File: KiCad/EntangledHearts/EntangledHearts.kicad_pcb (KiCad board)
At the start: 2 copper layers, 63 parts, among them J1 Conn_01x05_Pin, J2 MPU, J3 USB4135-GF-A, J4 OLED Display, J5 Conn_01x05_Pin, J6 Conn_01x05_Pin, Q1 SFH_3711, Q3 2N7002, Q4 2N7002, U1 ESP32-S3-WROOM-1, U2 MCP73831-2-OT, U3 TC1185-xCT

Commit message: ADD: first pcbs added
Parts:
- removed S_BOOT1, S_TXD2: TXD, TestPoint:TestPoint_Pad_1.0x1.0mm
- removed S_BOOT2: Boot, TestPoint:TestPoint_Pad_1.0x1.0mm
- removed S_EN1, S_RXD2: RXD, TestPoint:TestPoint_Pad_1.0x1.0mm
- removed S_EN2: Enabled, TestPoint:TestPoint_Pad_1.0x1.0mm
- removed S_RXD1: DTR, TestPoint:TestPoint_Pad_1.0x1.0mm
- removed S_TXD1: RTS, TestPoint:TestPoint_Pad_1.0x1.0mm
- removed TPS_GND1, TPS_GND2: GND, TestPoint:TestPoint_Pad_1.0x1.0mm
- +Bat1: renamed from TP16; footprint TestPoint:TestPoint_Pad_1.0x1.0mm -> TestPoint:TestPoint_Pad_2.5x2.5mm
- -Bat1: renamed from TP4; footprint TestPoint:TestPoint_Pad_1.0x1.0mm -> TestPoint:TestPoint_Pad_2.5x2.5mm
- Seriell_Flash1: renamed from J6; value Conn_01x05_Pin -> Flash
- Seriell_Input1: renamed from J1; value Conn_01x05_Pin -> Input
- Seriell_Output1: renamed from J5; value Conn_01x05_Pin -> Output
- moved S2 121.1 mm to (226.1, 103.9)
- moved C12 109.7 mm to (239.7, 121.5)
- moved C15 109.2 mm to (242.2, 116.4)
- moved U3 101.8 mm to (216.0, 114.8)
- moved C14 101.6 mm to (234.9, 111.3)
- moved C13 101.3 mm to (230.8, 117.7)
- moved R7 94.9 mm to (232.1, 130.4)
- moved U2 87.8 mm to (201.0, 112.7), turned to 90 degrees
- moved J3 84.3 mm to (187.3, 115.2), turned to -90 degrees
- moved Seriell_Output1 84.0 mm to (213.0, 44.5)
- moved R9 83.9 mm to (201.9, 40.6)
- moved R10 79.5 mm to (191.8, 40.6)
- moved -Bat1 79.2 mm to (208.3, 124.0)
- moved C11 77.6 mm to (205.7, 117.7), turned to -90 degrees
- moved +Bat1 73.4 mm to (208.3, 106.3)
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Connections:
- C8 pad 2: Net-(U1-GPIO0/BOOT) -> Net-(Seriell_Flash1-Pin_1)
- C9 pad 2: Net-(U1-EN) -> Net-(Seriell_Flash1-Pin_4)
- R5 pad 1: Net-(U1-GPIO0/BOOT) -> Net-(Seriell_Flash1-Pin_1)
- R6 pad 1: Net-(U1-EN) -> Net-(Seriell_Flash1-Pin_4)
- Seriell_Flash1 pad 1: unconnected-(J6-Pin_1-Pad1) -> Net-(Seriell_Flash1-Pin_1)
- Seriell_Flash1 pad 2: unconnected-(J6-Pin_2-Pad2) -> Net-(Seriell_Flash1-Pin_2)
- Seriell_Flash1 pad 3: unconnected-(J6-Pin_3-Pad3) -> Net-(Seriell_Flash1-Pin_3)
- Seriell_Flash1 pad 4: unconnected-(J6-Pin_4-Pad4) -> Net-(Seriell_Flash1-Pin_4)
- Seriell_Flash1 pad 5: unconnected-(J6-Pin_5-Pad5) -> GND
- Seriell_Input1 pad 1: unconnected-(J1-Pin_1-Pad1) -> Net-(Q4-S)
- Seriell_Input1 pad 2: unconnected-(J1-Pin_2-Pad2) -> Net-(Q3-S)
- Seriell_Input1 pad 3: unconnected-(J1-Pin_3-Pad3) -> Net-(Seriell_Input1-Pin_3)
- Seriell_Input1 pad 4: unconnected-(J1-Pin_4-Pad4) -> Net-(Seriell_Input1-Pin_4)
- Seriell_Input1 pad 5: unconnected-(J1-Pin_5-Pad5) -> Net-(Seriell_Input1-Pin_5)
- Seriell_Output1 pad 1: unconnected-(J5-Pin_1-Pad1) -> Net-(Q3-D)
- Seriell_Output1 pad 2: unconnected-(J5-Pin_2-Pad2) -> Net-(Seriell_Input1-Pin_3)
- Seriell_Output1 pad 3: unconnected-(J5-Pin_3-Pad3) -> Net-(Seriell_Input1-Pin_4)
- Seriell_Output1 pad 4: unconnected-(J5-Pin_4-Pad4) -> Net-(Q4-D)
- Seriell_Output1 pad 5: unconnected-(J5-Pin_5-Pad5) -> Net-(Seriell_Input1-Pin_5)
- U1 pad 27: Net-(U1-GPIO0/BOOT) -> Net-(Seriell_Flash1-Pin_1)
- U1 pad 3: Net-(U1-EN) -> Net-(Seriell_Flash1-Pin_4)
- U1 pad 36: Net-(U1-U0RXD/GPIO44/CLK_OUT2) -> Net-(Seriell_Flash1-Pin_2)
- U1 pad 37: Net-(U1-U0TXD/GPIO43/CLK_OUT1) -> Net-(Seriell_Flash1-Pin_3)
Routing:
- net GND: track 0.00 -> 55.2 mm
- net Net-(Seriell_Input1-Pin_3): track 0.00 -> 36.6 mm, vias 0 -> 2
- net Net-(Seriell_Input1-Pin_5): track 0.00 -> 32.2 mm
- net Net-(Seriell_Input1-Pin_4): track 0.00 -> 30.0 mm, vias 0 -> 2
- net Net-(Q4-S): track 0.00 -> 29.8 mm, vias 0 -> 3
- net Net-(Q3-S): track 0.00 -> 26.3 mm
- net Net-(U2-V_{DD}): track 0.00 -> 25.8 mm
- net Net-(Q4-D): track 0.00 -> 23.9 mm
- net Net-(Q3-D): track 0.00 -> 15.5 mm
- net Net-(U2-V_{BAT}): track 0.00 -> 15.1 mm
- net Net-(Q4-G): track 0.00 -> 4.67 mm
- net Net-(Q3-G): track 0.00 -> 4.67 mm
- net Net-(D7-A): track 0.00 -> 3.04 mm
- net Net-(D7-K): track 0.00 -> 2.24 mm

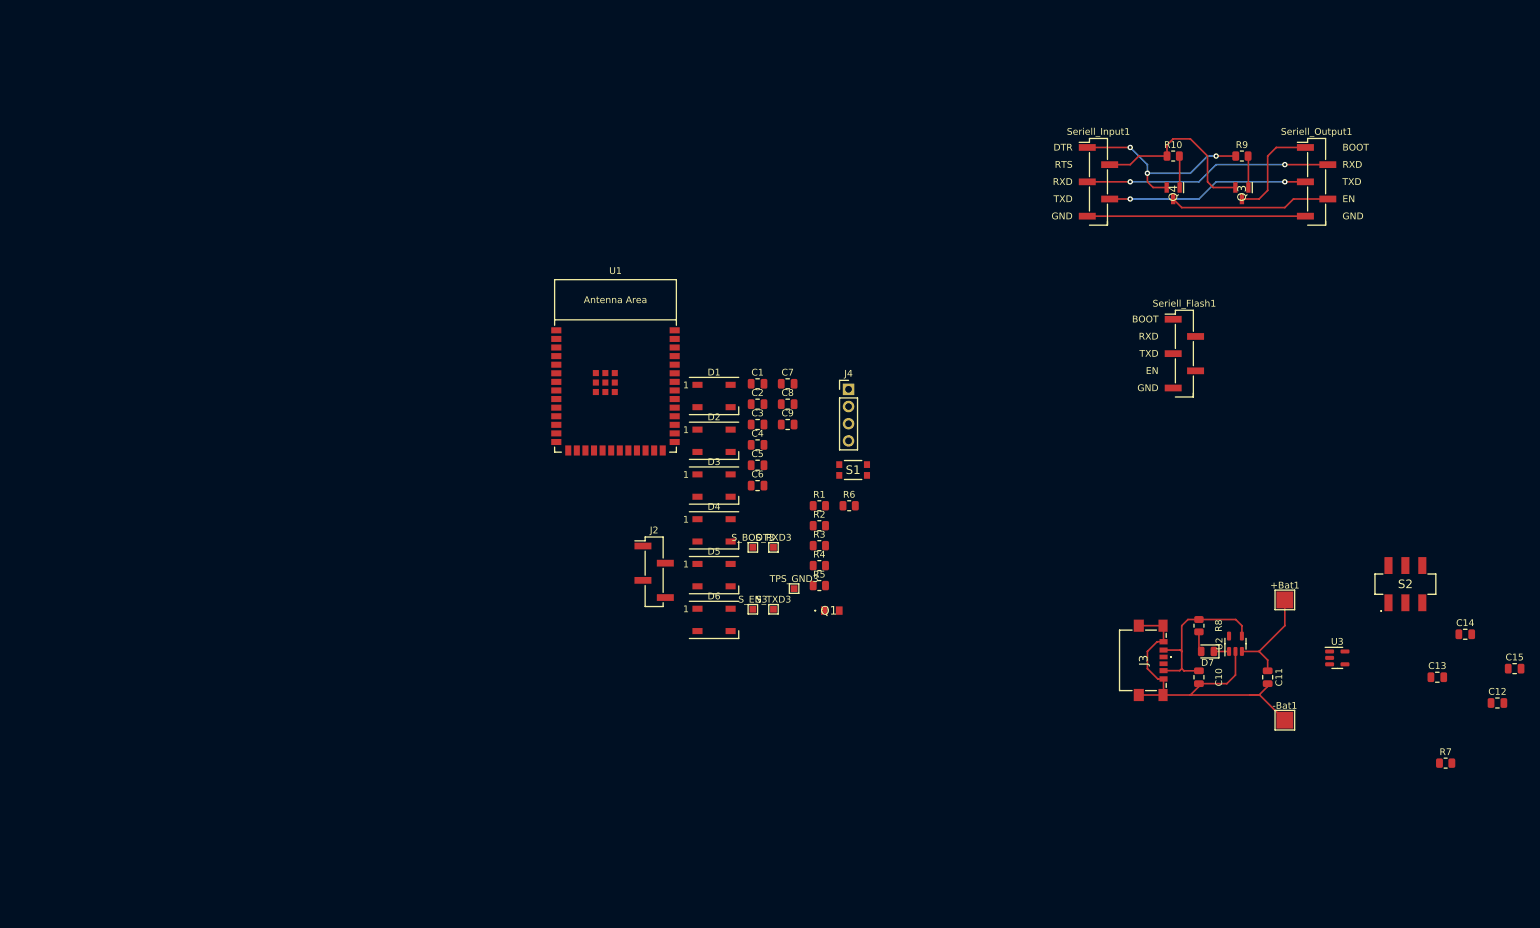
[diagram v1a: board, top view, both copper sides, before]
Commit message: CHG cleanup of Schematics done
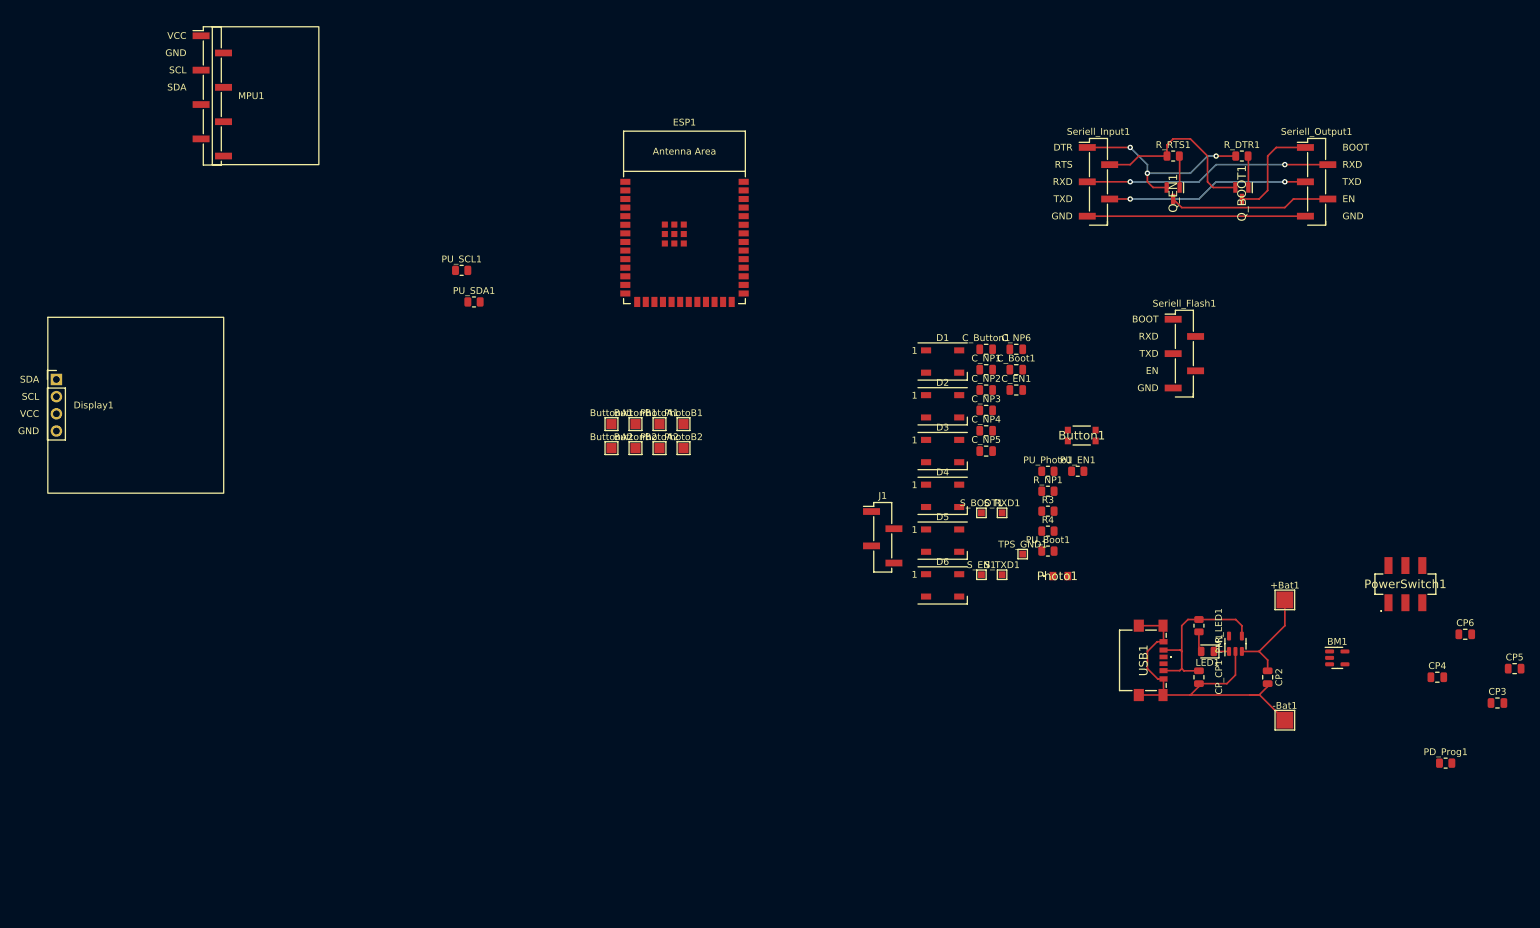
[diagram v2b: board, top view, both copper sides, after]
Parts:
- added ButtonA1: ButtonA1, TestPoint:TestPoint_Pad_1.5x1.5mm, F.Cu at (108.7, 80.3)
- added ButtonA2: ButtonA2, TestPoint:TestPoint_Pad_1.5x1.5mm, F.Cu at (108.7, 83.8)
- added ButtonB1: ButtonB1, TestPoint:TestPoint_Pad_1.5x1.5mm, F.Cu at (112.3, 80.3)
- added ButtonB2: ButtonB2, TestPoint:TestPoint_Pad_1.5x1.5mm, F.Cu at (112.3, 83.8)
- added MPU1: Conn_01x08_Pin, Connector_PinHeader_2.54mm:PinHeader_1x08_P2.54mm_Vertical_SMD_Pin1Left, F.Cu at (49.7, 31.8)
- added PU_SCL1: 10kΩ, Resistor_SMD:R_0805_2012Metric, F.Cu at (86.6, 57.5)
- added PU_SDA1: 10kΩ, Resistor_SMD:R_0805_2012Metric, F.Cu at (88.4, 62.2)
- added PhotoA1: PhotoA1, TestPoint:TestPoint_Pad_1.5x1.5mm, F.Cu at (115.8, 80.3)
- added PhotoA2: PhotoA2, TestPoint:TestPoint_Pad_1.5x1.5mm, F.Cu at (115.8, 83.8)
- added PhotoB1: PhotoB1, TestPoint:TestPoint_Pad_1.5x1.5mm, F.Cu at (119.4, 80.3)
- added PhotoB2: PhotoB2, TestPoint:TestPoint_Pad_1.5x1.5mm, F.Cu at (119.4, 83.8)
- D1: value WS2812B -> NP1
- D2: value WS2812B -> NP2
- D3: value WS2812B -> NP3
- D4: value WS2812B -> NP4
- D5: value WS2812B -> NP5
- D6: value WS2812B -> NP6
- moved Display1 117.1 mm to (26.7, 73.7)
- moved Button1 34.2 mm to (178.2, 82.0)
- moved C_Button1 34.2 mm to (164.1, 69.2)
- moved C_NP1 34.2 mm to (164.1, 72.2)
- moved C_NP2 34.2 mm to (164.1, 75.2)
- moved C_NP3 34.2 mm to (164.1, 78.2)
- moved C_NP4 34.2 mm to (164.1, 81.2)
- moved C_NP5 34.2 mm to (164.1, 84.3)
- moved J1 34.2 mm to (148.8, 97.0)
- moved S_BOOT1 34.2 mm to (163.4, 93.4)
- moved S_EN1 34.2 mm to (163.4, 102.5)
- moved TPS_GND1 34.2 mm to (169.5, 99.5)
- moved D1 34.2 mm to (157.7, 71.0)
- moved D2 34.2 mm to (157.7, 77.6)
- moved D3 34.2 mm to (157.7, 84.3)
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- renumbered U3 to BM1, S1 to Button1, C11 to CP2, C12 to CP3, C13 to CP4, C15 to CP5, C14 to CP6, C10 to CP_CP1, C8 to C_Boot1, C1 to C_Button1, C9 to C_EN1, C2 to C_NP1, C3 to C_NP2, C4 to C_NP3, C5 to C_NP4, C6 to C_NP5, C7 to C_NP6, J4 to Display1, U1 to ESP1, J2 to J1, D7 to LED1, R7 to PD_Prog1, U2 to PM1, R5 to PU_Boot1, R6 to PU_EN1, R1 to PU_Photo1, Q1 to Photo1, S2 to PowerSwitch1, Q3 to Q_BOOT1, Q4 to Q_EN1, R9 to R_DTR1, R8 to R_LED1, R2 to R_NP1, R10 to R_RTS1, S_BOOT3 to S_BOOT1, S_EN3 to S_EN1, S_RXD3 to S_RXD1, S_TXD3 to S_TXD1, TPS_GND3 to TPS_GND1, J3 to USB1
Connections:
- net Net-(Seriell_Flash1-Pin_1) renamed Boot
- net Net-(Seriell_Flash1-Pin_4) renamed EN
- net Net-(U1-GPIO21) renamed NeoPixel
- Button1 pad 3: GND -> Net-(Button1-Pad3)
- Button1 pad 4: Net-(U1-GPIO1/TOUCH1/ADC1_CH0) -> Net-(Button1-Pad4)
- C_Button1 pad 1: Net-(U1-GPIO1/TOUCH1/ADC1_CH0) -> Button
- Display1 pad 1: GND -> SDA
- Display1 pad 2: +4V -> SCL
- Display1 pad 3: Net-(J2-Pin_2) -> +4V
- Display1 pad 4: Net-(J2-Pin_1) -> GND
- ESP1 pad 19: Net-(J2-Pin_1) -> SCL
- ESP1 pad 20: Net-(J2-Pin_2) -> SDA
- ESP1 pad 36: Net-(Seriell_Flash1-Pin_2) -> TXD
- ESP1 pad 37: Net-(Seriell_Flash1-Pin_3) -> RXD
- ESP1 pad 38: Net-(Q1-C) -> Photo
- ESP1 pad 39: Net-(U1-GPIO1/TOUCH1/ADC1_CH0) -> Button
- J1 pad 1: Net-(J2-Pin_1) -> SCL
- J1 pad 2: Net-(J2-Pin_2) -> SDA
- PU_Photo1 pad 1: Net-(Q1-C) -> Photo
- PU_Photo1 pad 2: +3.3V -> unconnected-(PU_Photo1-Pad2)
- Photo1 pad 1: GND -> Net-(Photo1-E)
- Photo1 pad 2: Net-(Q1-C) -> Net-(Photo1-C)
- R3 pad 1: Net-(J2-Pin_1) -> SCL
- R4 pad 1: Net-(J2-Pin_2) -> SDA
- Seriell_Flash1 pad 2: Net-(Seriell_Flash1-Pin_2) -> RXD
- Seriell_Flash1 pad 3: Net-(Seriell_Flash1-Pin_3) -> TXD

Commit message: ADD: further progress
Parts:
- removed J1: MPU, Connector_PinHeader_2.54mm:PinHeader_1x04_P2.54mm_Vertical_SMD_Pin1Left
- removed R3, R4: 10kΩ, Resistor_SMD:R_0805_2012Metric
- removed S_BOOT1: Boot, TestPoint:TestPoint_Pad_1.0x1.0mm
- removed S_EN1: Enabled, TestPoint:TestPoint_Pad_1.0x1.0mm
- removed S_RXD1: RXD (twist), TestPoint:TestPoint_Pad_1.0x1.0mm
- removed S_TXD1: TXD (twist), TestPoint:TestPoint_Pad_1.0x1.0mm
- removed TPS_GND1: GND, TestPoint:TestPoint_Pad_1.0x1.0mm
- added GND1: GND1, TestPoint:TestPoint_Pad_1.5x1.5mm, B.Cu at (96.5, 20.3)
- added GND2: GND2, TestPoint:TestPoint_Pad_1.5x1.5mm, B.Cu at (207.0, 80.4)
- added NeoPixel1: NeoPixel1, TestPoint:TestPoint_Pad_1.5x1.5mm, B.Cu at (88.9, 20.3)
- added NeoPixel2: NeoPixel2, TestPoint:TestPoint_Pad_1.5x1.5mm, B.Cu at (222.2, 80.4)
- added SCL1: SCL1, TestPoint:TestPoint_Pad_1.5x1.5mm, B.Cu at (85.1, 20.3)
- added SCL2: SCL2, TestPoint:TestPoint_Pad_1.5x1.5mm, B.Cu at (214.6, 80.4)
- added SDA1: SDA1, TestPoint:TestPoint_Pad_1.5x1.5mm, B.Cu at (81.3, 20.3)
- added SDA2: SDA2, TestPoint:TestPoint_Pad_1.5x1.5mm, B.Cu at (218.4, 80.4)
- added VCC1: VCC1, TestPoint:TestPoint_Pad_1.5x1.5mm, B.Cu at (92.7, 20.3)
- added VCC2: VCC2, TestPoint:TestPoint_Pad_1.5x1.5mm, B.Cu at (210.8, 80.4)
- +Bat1, -Bat1, ButtonA1, ButtonA2, ButtonB1, ButtonB2, CP_CP1, C_Button1, C_NP1, C_NP2, C_NP3, C_NP4, C_NP5, C_NP6, PU_Photo1, PhotoA1, PhotoA2, PhotoB1, PhotoB2, R_NP1: moved to B.Cu
- moved Display1 191.8 mm to (218.4, 75.3), turned to -90 degrees
- moved CP3 190.1 mm to (54.7, 78.1)
- moved CP6 189.9 mm to (48.0, 78.1)
- moved CP5 186.0 mm to (59.7, 80.6)
- moved PowerSwitch1 182.3 mm to (44.3, 90.8), turned to 90 degrees
- moved PD_Prog1 175.3 mm to (61.0, 92.0), turned to -90 degrees
- moved CP4 172.6 mm to (61.0, 87.0), turned to 90 degrees
- moved -Bat1 169.7 mm to (40.7, 97.1), turned to 180 degrees
- moved BM1 161.1 mm to (57.3, 87.0)
- moved CP_CP1 151.2 mm to (45.8, 97.1), turned to 180 degrees
- moved +Bat1 150.1 mm to (58.5, 97.1), turned to 180 degrees
- moved LED1 146.6 mm to (52.1, 90.8), turned to 90 degrees
- moved PM1 145.1 mm to (57.3, 92.4), turned to 0 degrees
- moved R_LED1 144.5 mm to (53.4, 84.4), turned to 180 degrees
- moved CP2 143.9 mm to (63.5, 95.8), turned to 90 degrees
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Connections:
- Button1 pad 2: unconnected-(Button1-Pad2) -> Net-(Button1-Pad2)
- Button1 pad 3: Net-(Button1-Pad3) -> unconnected-(Button1-Pad3)
- ButtonB2 pad 1: Net-(Button1-Pad3) -> Net-(Button1-Pad2)
- C_NP1 pad 1: +4V -> VCC_Top
- C_NP1 pad 2: GND -> GND_Top
- C_NP2 pad 1: +4V -> VCC_Top
- C_NP2 pad 2: GND -> GND_Top
- C_NP3 pad 1: +4V -> VCC_Top
- C_NP3 pad 2: GND -> GND_Top
- C_NP4 pad 1: +4V -> VCC_Top
- C_NP4 pad 2: GND -> GND_Top
- C_NP5 pad 1: +4V -> VCC_Top
- C_NP5 pad 2: GND -> GND_Top
- C_NP6 pad 1: +4V -> VCC_Top
- C_NP6 pad 2: GND -> GND_Top
- D1 pad 1: +4V -> VCC_Top
- D1 pad 3: GND -> GND_Top
- D2 pad 1: +4V -> VCC_Top
- D2 pad 3: GND -> GND_Top
- D3 pad 1: +4V -> VCC_Top
- D3 pad 3: GND -> GND_Top
- D4 pad 1: +4V -> VCC_Top
- D4 pad 3: GND -> GND_Top
- D5 pad 1: +4V -> VCC_Top
- D5 pad 3: GND -> GND_Top
- D6 pad 1: +4V -> VCC_Top
- D6 pad 3: GND -> GND_Top
- Display1 pad 1: SDA -> SDA_Top
- Display1 pad 2: SCL -> SCL_Top
- Display1 pad 3: +4V -> VCC_Top
- Display1 pad 4: GND -> GND_Top
- ESP1 pad 19: SCL -> SDA_Bottom
- ESP1 pad 20: SDA -> SCL_Bottom
- ESP1 pad 23: NeoPixel -> NeoPixelBottom
- MPU1 pad 3: SCL -> SCL_Bottom
- MPU1 pad 4: SDA -> SDA_Bottom
- PU_Photo1 pad 2: unconnected-(PU_Photo1-Pad2) -> +3.3V
- PU_SCL1 pad 1: SCL -> SCL_Bottom
- PU_SDA1 pad 1: SDA -> SDA_Bottom
- R_NP1 pad 1: NeoPixel -> NeoPixel_Top
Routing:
- net VCC_Top: track 0.00 -> 152.3 mm, vias 0 -> 7
- net GND_Top: track 0.00 -> 151.2 mm, vias 0 -> 6
- net GND: track 55.2 -> 171.8 mm, vias 0 -> 3
- net EN: track 0.00 -> 28.7 mm, vias 0 -> 2
- net Net-(D1-DOUT): track 0.00 -> 22.1 mm
- net Net-(D4-DOUT): track 0.00 -> 21.6 mm
- net Net-(D5-DOUT): track 0.00 -> 21.3 mm
- net Net-(D3-DOUT): track 0.00 -> 19.2 mm
- net Net-(D2-DOUT): track 0.00 -> 18.5 mm
- net RXD: track 0.00 -> 15.0 mm
- net +4V: track 0.00 -> 13.9 mm
- net TXD: track 0.00 -> 13.0 mm, vias 0 -> 2
- net Boot: track 0.00 -> 11.5 mm
- net Net-(Button1-Pad4): track 0.00 -> 6.36 mm, vias 0 -> 1
- net Net-(Button1-Pad2): track 0.00 -> 6.36 mm, vias 0 -> 1
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
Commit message: CHG: some minor changes
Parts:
- MPU1: moved to B.Cu
- moved MPU1 184.6 mm to (214.6, 94.4), turned to 90 degrees
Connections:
- MPU1 pad 1: +4V -> VCC_Top
- MPU1 pad 2: GND -> GND_Top
- MPU1 pad 3: SCL_Bottom -> SCL_Top
- MPU1 pad 4: SDA_Bottom -> SDA_Top

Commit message: ADD: all parts connected
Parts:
- removed +Bat1: + Bat, TestPoint:TestPoint_Pad_2.5x2.5mm
- removed -Bat1: - Bat, TestPoint:TestPoint_Pad_2.5x2.5mm
- added BatteryConnector1: BatteryConnector, Connector_JST:JST_PH_S2B-PH-SM4-TB_1x02-1MP_P2.00mm_Horizontal, B.Cu at (111.0, 129.9)
- CP2, PD_Prog1, PU_Boot1, PU_EN1, PU_SCL1, PU_SDA1: moved to B.Cu
- CP_CP1: moved to F.Cu
- R_NP1: value 300Ω -> 330Ω
- moved GND1 108.1 mm to (101.6, 128.3), turned to 90 degrees
- moved VCC1 104.5 mm to (101.6, 124.5), turned to 90 degrees
- moved NeoPixel1 101.1 mm to (101.6, 120.7), turned to -90 degrees
- moved Seriell_Flash1 99.1 mm to (139.3, 127.0)
- moved SCL1 97.9 mm to (101.6, 116.8), turned to 90 degrees
- moved SDA1 94.9 mm to (101.6, 113.0), turned to 90 degrees
- moved R_LED1 91.6 mm to (124.5, 142.2)
- moved ESP1 89.4 mm to (120.8, 111.1)
- moved PowerSwitch1 89.0 mm to (124.5, 129.3), turned to 0 degrees
- moved CP_CP1 85.6 mm to (118.4, 142.4)
- moved USB1 84.9 mm to (120.7, 149.3)
- moved BM1 84.9 mm to (128.4, 138.8)
- moved LED1 84.9 mm to (123.2, 137.2), turned to -90 degrees
- moved PD_Prog1 84.5 mm to (130.8, 139.7)
- moved CP6 84.1 mm to (112.1, 132.5), turned to 90 degrees
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- renumbered PM1 to BM1, BM1 to PM1
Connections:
- ESP1 pad 11: unconnected-(ESP1-GPIO18/U1RXD/ADC2_CH7/CLK_OUT3-Pad11) -> NeoPixel_Bottom
- ESP1 pad 23: NeoPixelBottom -> unconnected-(ESP1-GPIO21-Pad23)
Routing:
- net +3.3V: track 0.00 -> 65.7 mm, vias 0 -> 2
- net +4V: track 13.9 -> 50.1 mm, vias 0 -> 2
- net SCL_Bottom: track 0.00 -> 31.1 mm, vias 0 -> 2
- net SDA_Bottom: track 0.00 -> 25.0 mm, vias 0 -> 1
- net GND: track 171.8 -> 196.6 mm, vias 3 -> 7
- net Boot: track 11.5 -> 32.7 mm, vias 0 -> 1
- net Button: track 4.47 -> 25.0 mm, vias 0 -> 1
- net Net-(BM1-V_{BAT}): track 15.3 -> 33.5 mm, vias 1 -> 3
- net RXD: track 15.0 -> 33.1 mm, vias 0 -> 2
- net EN: track 28.7 -> 45.9 mm, vias 2 -> 3
- net TXD: track 13.0 -> 26.0 mm
- net NeoPixel_Bottom: track 0.00 -> 12.5 mm, vias 0 -> 1
- net Photo: track 4.48 -> 13.4 mm, vias 0 -> 1
- net Net-(BM1-STAT): track 0.00 -> 4.73 mm
- net Net-(LED1-A): track 0.00 -> 4.29 mm
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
